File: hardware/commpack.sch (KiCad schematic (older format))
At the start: 12 parts, among them J1 1240COMM, J2 1240COMM_EXT, J3 L8BE-1G1T-91A, J4 USB_B, U3 27C128, U4 AP1117-33

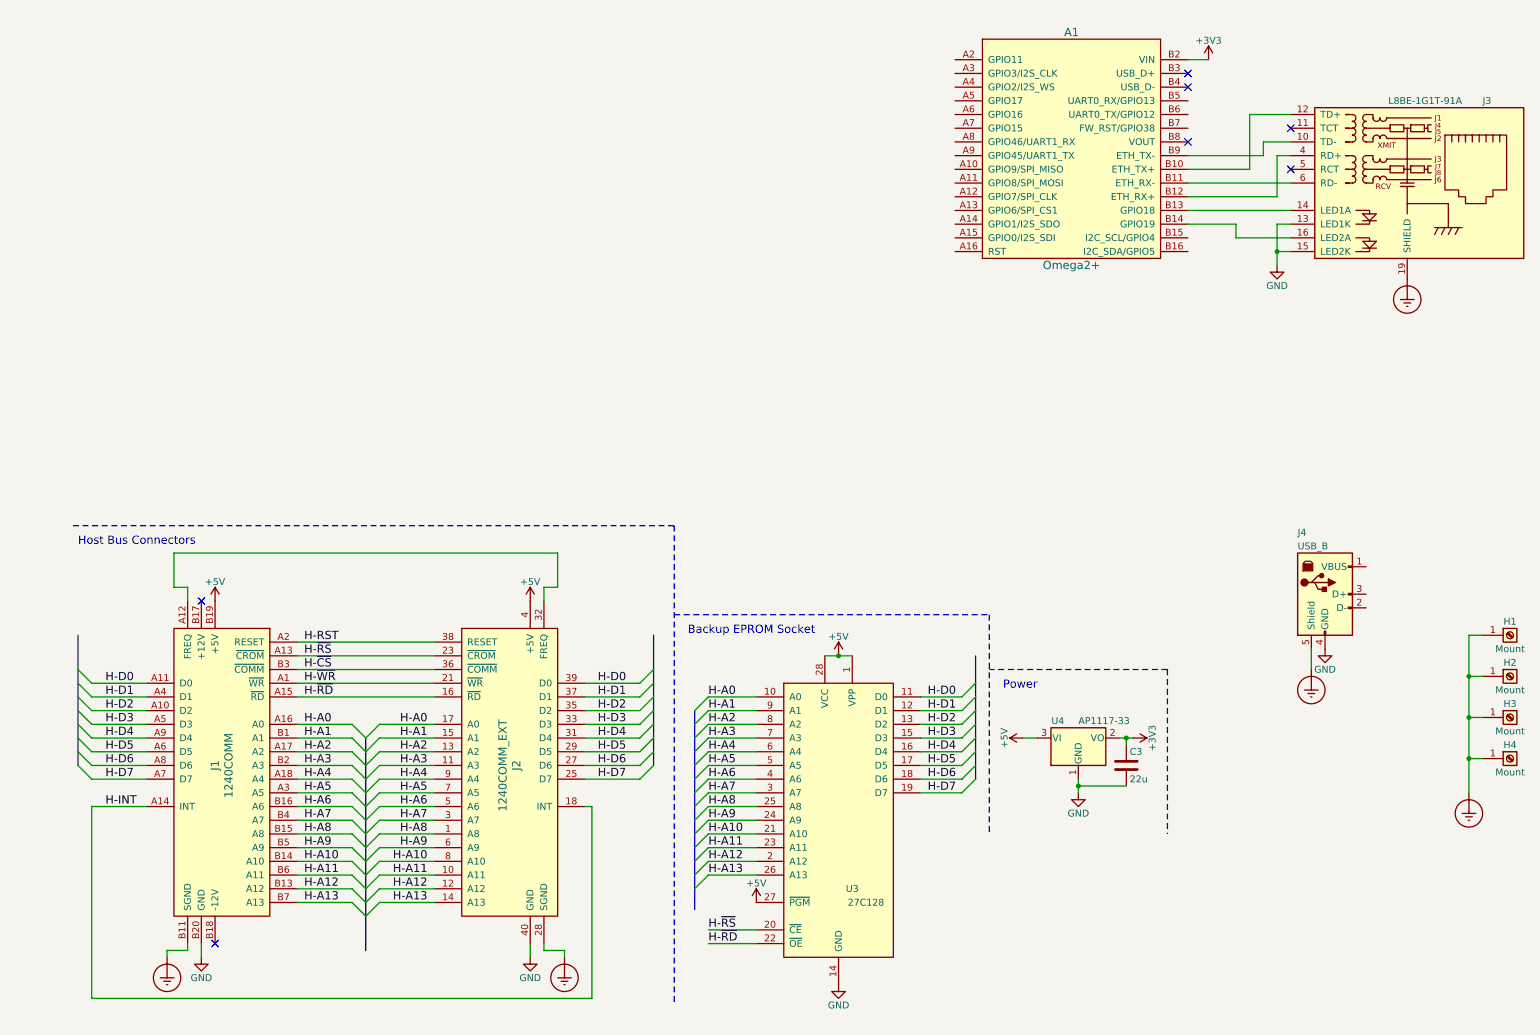
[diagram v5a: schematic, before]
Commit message: Add UART, flash ROM to schematic.
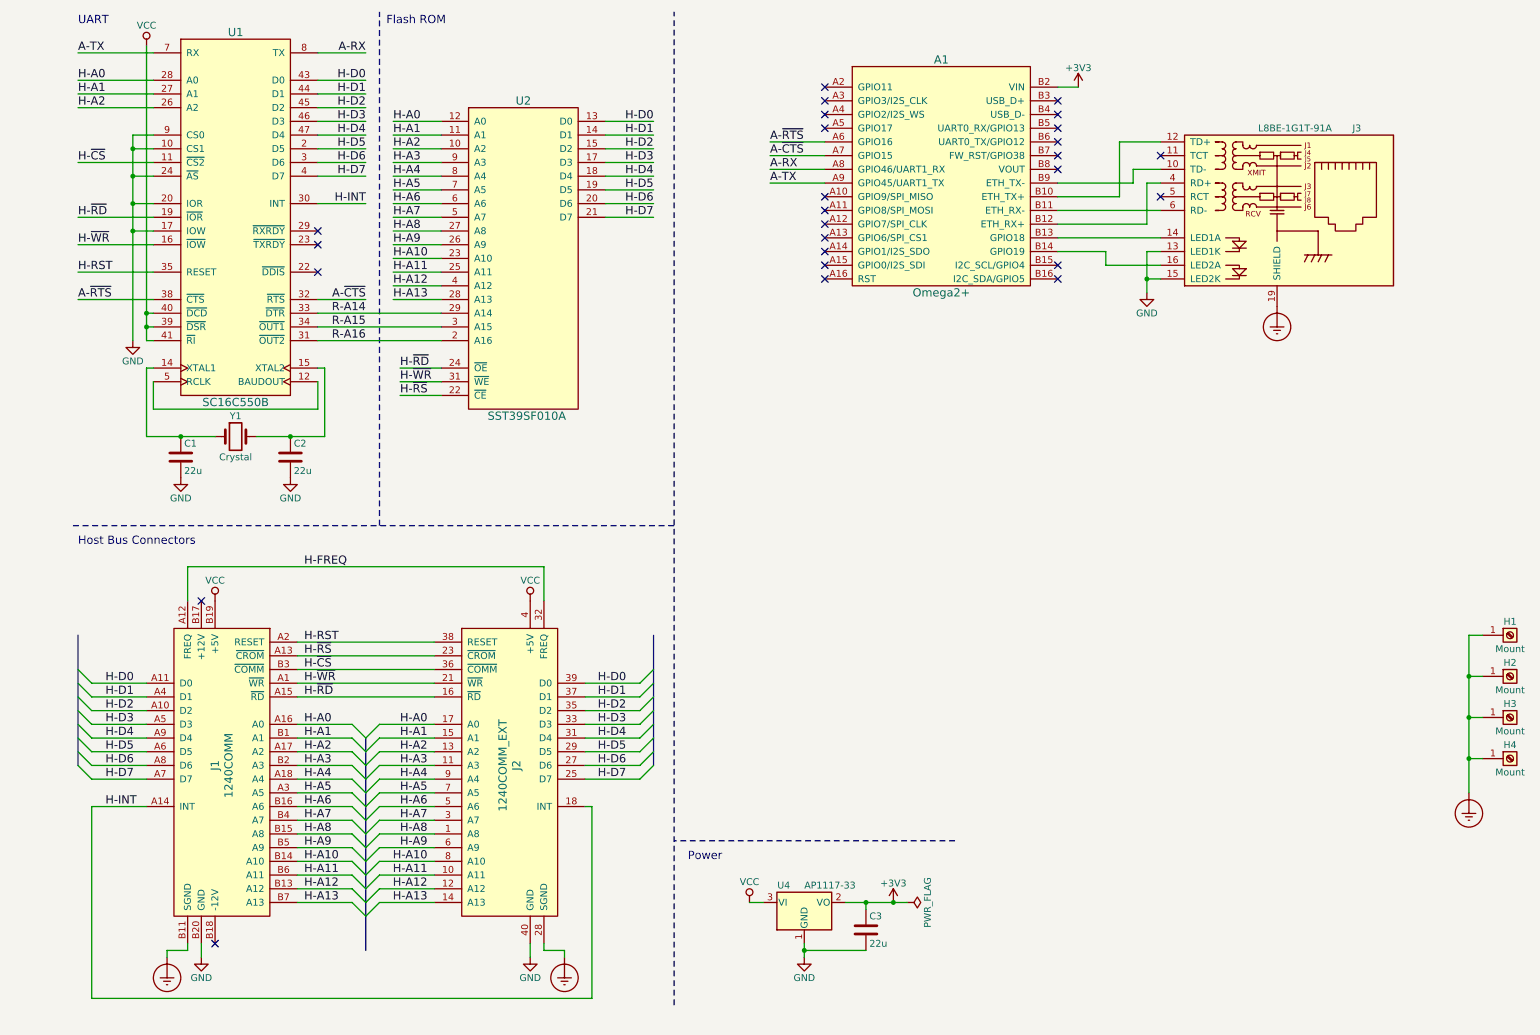
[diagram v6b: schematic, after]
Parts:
- removed J4: USB_B, ether1240:USB-B, symbol USB_B
- removed U3: 27C128, Housings_DIP:DIP-28_W15.24mm_Socket, symbol 27C128
- added C1, C2: 22u, Capacitors_SMD:C_0805_HandSoldering, symbol C
- added U1: SC16C550B, Housings_QFP:LQFP-48_7x7mm_Pitch0.5mm, symbol SC16C550B
- added U2: SST39SF010A, ether1240:PLCC-32_THT-Socket, symbol SST39SF010A
- added Y1: Crystal, Crystals:Crystal_SMD_HC49-SD_HandSoldering, symbol Crystal
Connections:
- net GND: now also C1.2, C2.2, U1.10 (CS1), U1.17 (IOW), U1.18 (GND), U1.20 (IOR), U1.24 (~AS), U1.9 (CS0), U2.16 (GND)
- net H-A0: now also U1.28 (A0), U2.12 (A0)
- net H-A1: now also U1.27 (A1), U2.11 (A1)
- net H-A10: now also U2.23 (A10)
- net H-A11: now also U2.25 (A11)
- net H-A12: now also U2.4 (A12)
- net H-A13: now also U2.28 (A13)
- net H-A2: now also U1.26 (A2), U2.10 (A2)
- net H-A3: now also U2.9 (A3)
- net H-A4: now also U2.8 (A4)
- net H-A5: now also U2.7 (A5)
- net H-A6: now also U2.6 (A6)
- net H-A7: now also U2.5 (A7)
- net H-A8: now also U2.27 (A8)
- net H-A9: now also U2.26 (A9)
- net H-D0: now also U1.43 (D0), U2.13 (D0)
- net H-D1: now also U1.44 (D1), U2.14 (D1)
- net H-D2: now also U1.45 (D2), U2.15 (D2)
- net H-D3: now also U1.46 (D3), U2.17 (D3)
- net H-D4: now also U1.47 (D4), U2.18 (D4)
- net H-D5: now also U1.2 (D5), U2.19 (D5)
- net H-D6: now also U1.3 (D6), U2.20 (D6)
- net H-D7: now also U1.4 (D7), U2.21 (D7)
- net H-INT: now also U1.30 (INT)
- net H-RST: now also U1.35 (RESET)
- net H-~CS: now also U1.11 (~CS2)
- net H-~RD: now also U1.19 (~IOR), U2.24 (~OE)
- net H-~RS: now also U2.22 (~CE)
- net H-~WR: now also U1.16 (~IOW), U2.31 (~WE)
- net H-FREQ: now reaches J1.A12 (FREQ), J2.32 (FREQ)
- net A-~RTS: now reaches A1.A6 (GPIO16)
- net A-~RTS: now also U1.38 (~CTS)
- net A-~CTS: now reaches A1.A7 (GPIO15)
- net A-~CTS: now also U1.32 (~RTS)
- net A-RX: now reaches A1.A8 (GPIO46/UART1_RX)
- net A-RX: now also U1.8 (TX)
- net A-TX: now reaches A1.A9 (GPIO45/UART1_TX)
- net A-TX: now also U1.7 (RX)
- net +5V renamed VCC
- net VCC: now also U1.39 (~DSR), U1.40 (~DCD), U1.41 (~RI), U1.42 (VCC), U2.32 (VCC)
- new net: U1.12 (BAUDOUT), U1.5 (RCLK)
- new net: C1.1, U1.14 (XTAL1), Y1.1
- new net: C2.1, U1.15 (XTAL2), Y1.2
- new net R-A14: U1.33 (~DTR), U2.29 (A14)
- new net R-A15: U1.34 (~OUT1), U2.3 (A15)
- new net R-A16: U1.31 (~OUT2), U2.2 (A16)
- no-connect marks 7 -> 26
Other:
- note added: "Flash ROM"
- note added: "UART"
- note removed: "Backup EPROM Socket"
- moved on the sheet: A1, C3, J3, U4

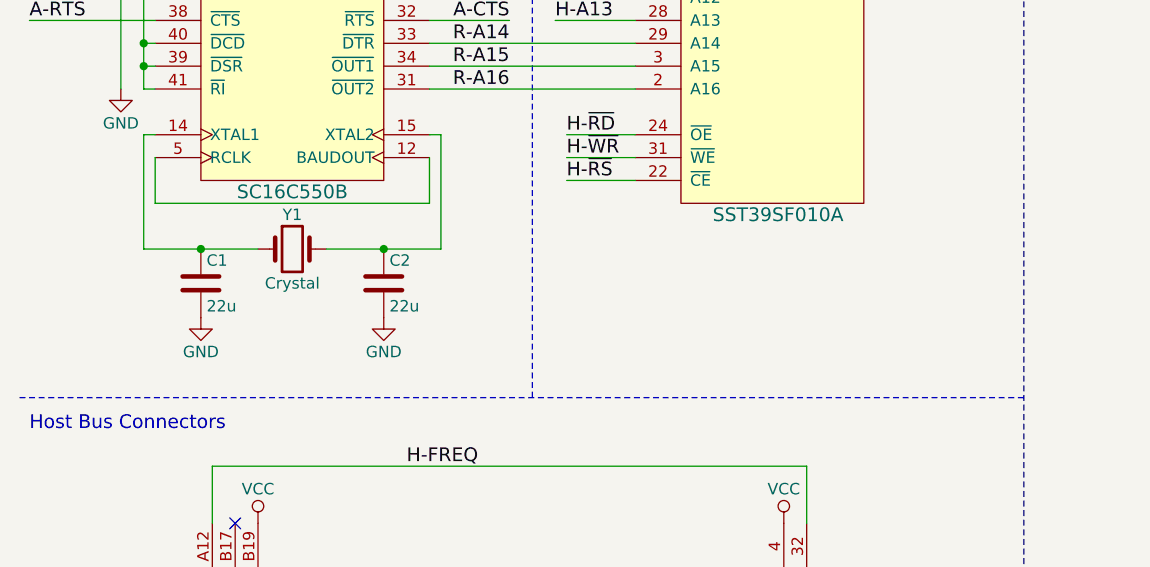
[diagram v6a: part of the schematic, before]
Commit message: Add decoupling caps on UART and ROM.
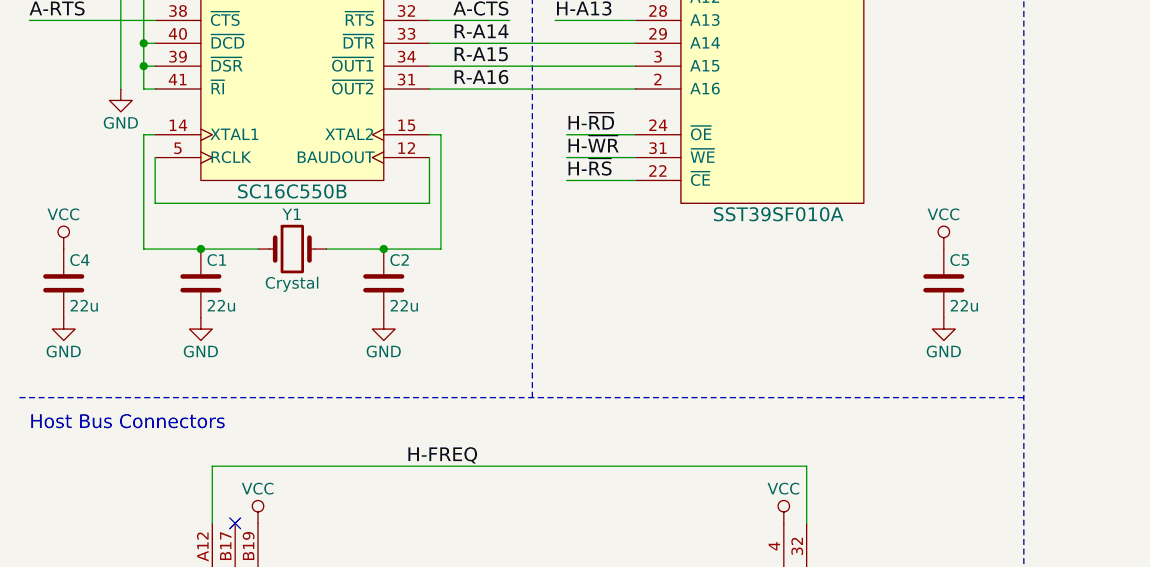
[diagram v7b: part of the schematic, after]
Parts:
- added C4, C5: 22u, Capacitors_SMD:C_0805_HandSoldering, symbol C
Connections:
- net GND: now also C4.2, C5.2
- net VCC: now also C4.1, C5.1
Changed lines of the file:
@@
 Text Label 5600 1750 0    60   ~ 0
 A-TX
+$Comp
+L C C4
+U 1 1 5A30FD8B
+P 700 3750
+F 0 "C4" H 725 3850 50  0000 L CNN
+F 1 "22u" H 725 3650 50  0000 L CNN
+F 2 "Capacitors_SMD:C_0805_HandSoldering" H 738 3600 50  0001 C CNN
+F 3 "" H 700 3750 50  0001 C CNN
+	1    700  3750
+	1    0    0    -1
+$EndComp
+$Comp
+L VCC #PWR019
+U 1 1 5A310545
+P 700 3600
+F 0 "#PWR019" H 700 3450 50  0001 C CNN
+F 1 "VCC" H 700 3750 50  0000 C CNN
+F 2 "" H 700 3600 50  0001 C CNN
+F 3 "" H 700 3600 50  0001 C CNN
+	1    700  3600
+	1    0    0    -1
+$EndComp
+$Comp
+L GND #PWR020
+U 1 1 5A310579
+P 700 3900
+F 0 "#PWR020" H 700 3650 50  0001 C CNN
+F 1 "GND" H 700 3750 50  0000 C CNN
+F 2 "" H 700 3900 50  0001 C CNN
+F 3 "" H 700 3900 50  0001 C CNN
+	1    700  3900
+	1    0    0    -1
+$EndComp
+$Comp
+L C C5
+U 1 1 5A31078C
+P 4550 3750
+F 0 "C5" H 4575 3850 50  0000 L CNN
+F 1 "22u" H 4575 3650 50  0000 L CNN
+F 2 "Capacitors_SMD:C_0805_HandSoldering" H 4588 3600 50  0001 C CNN
+F 3 "" H 4550 3750 50  0001 C CNN
+	1    4550 3750
+	1    0    0    -1
+$EndComp
+$Comp
+L VCC #PWR021
+U 1 1 5A310792
+P 4550 3600
+F 0 "#PWR021" H 4550 3450 50  0001 C CNN
+F 1 "VCC" H 4550 3750 50  0000 C CNN
+F 2 "" H 4550 3600 50  0001 C CNN
+F 3 "" H 4550 3600 50  0001 C CNN
+	1    4550 3600
+	1    0    0    -1
+$EndComp
+$Comp
+L GND #PWR022
+U 1 1 5A310798
+P 4550 3900
+F 0 "#PWR022" H 4550 3650 50  0001 C CNN
+F 1 "GND" H 4550 3750 50  0000 C CNN
+F 2 "" H 4550 3900 50  0001 C CNN
+F 3 "" H 4550 3900 50  0001 C CNN
+	1    4550 3900
+	1    0    0    -1
+$EndComp
 $EndSCHEMATC

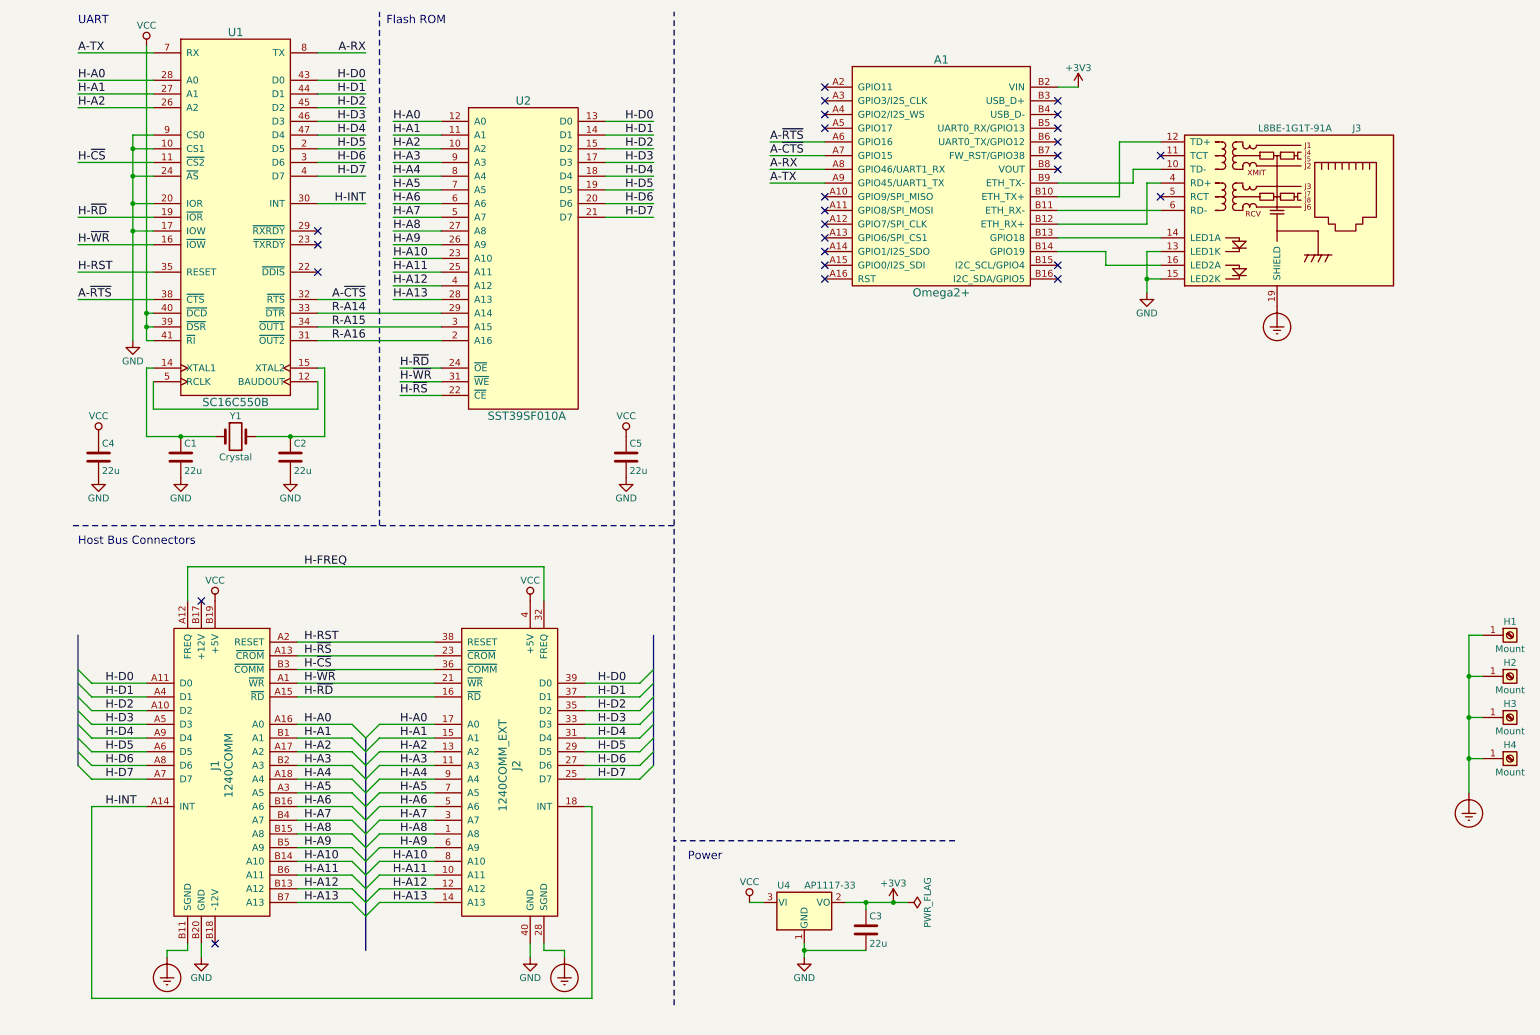
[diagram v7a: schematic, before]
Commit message: Add a level shifter on the serial lines to the Omega2.
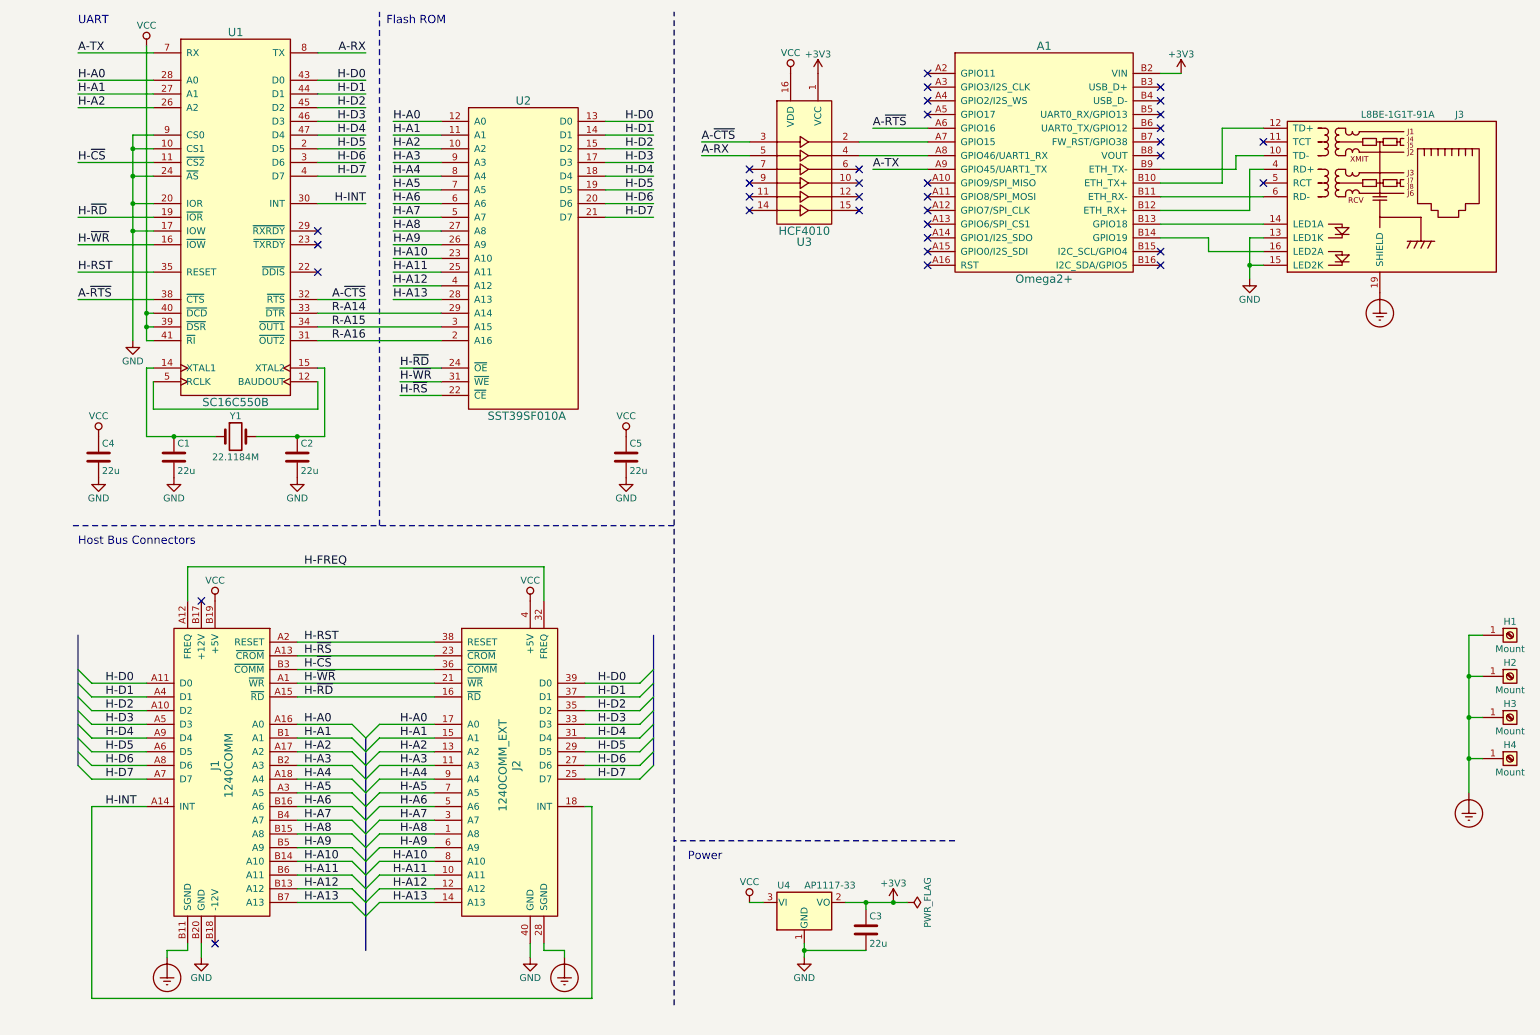
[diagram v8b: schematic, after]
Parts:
- added U3: HCF4010, Housings_SOIC:SOIC-16_3.9x9.9mm_Pitch1.27mm, symbol HCF4010
- Y1: value Crystal -> 22.1184M
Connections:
- net +3V3: now also U3.1 (VCC)
- net A-RX: now also U3.5; no longer A1.A8 (GPIO46/UART1_RX)
- net A-~CTS: now also U3.3; no longer A1.A7 (GPIO15)
- net GND: now also U3.8 (GND)
- net VCC: now also U3.16 (VDD)
- new net: A1.A7 (GPIO15), U3.2
- new net: A1.A8 (GPIO46/UART1_RX), U3.4
- no-connect marks 26 -> 34
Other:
- moved on the sheet: A1, C1, C2, J3
